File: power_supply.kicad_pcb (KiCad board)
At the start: 2 copper layers, 103.4 x 73 mm, 99 parts, among them J1 USB-IN, J2 USB OUT, Q1 SI4174DY, Q2 SI4463CDY, Q3 SI4463CDY, U1 LM3914, U10 FDC6392S, U11 MCP6041, U2 TPD2E001, U3 MIC2185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

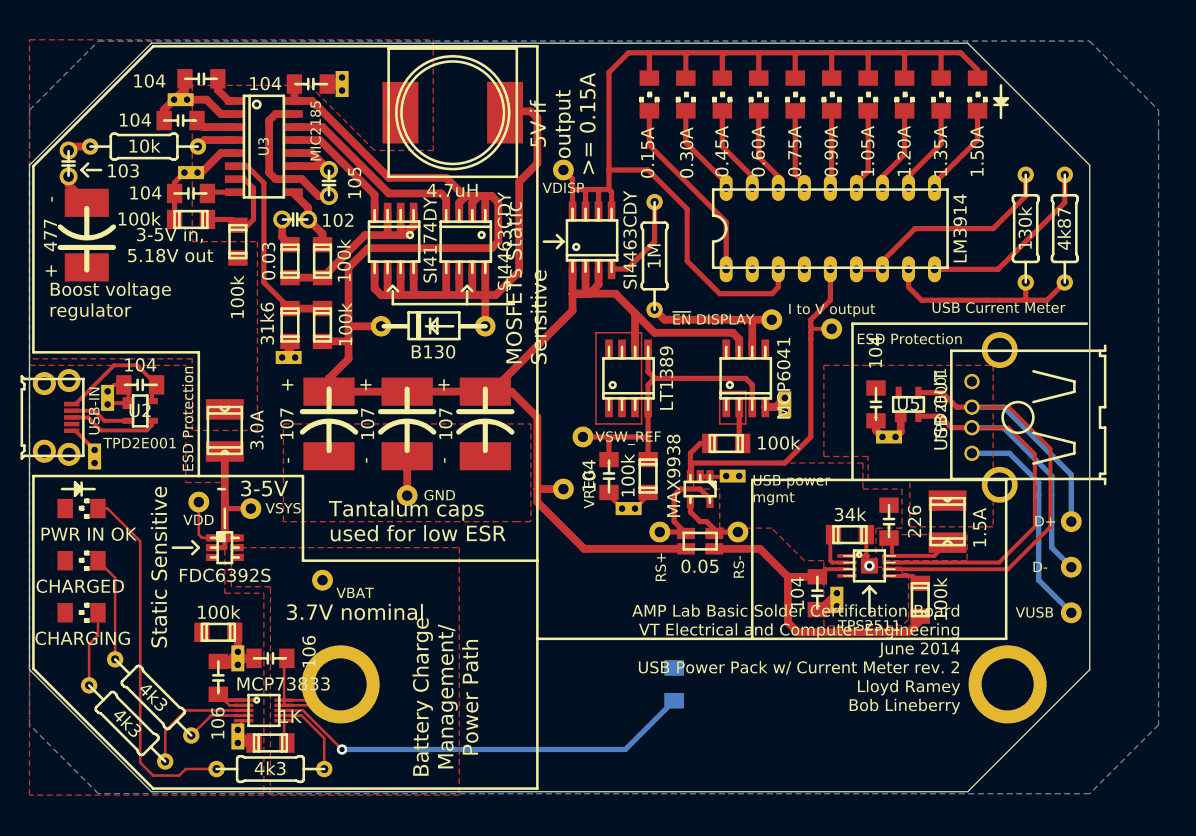
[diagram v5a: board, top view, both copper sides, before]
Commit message: Added test points
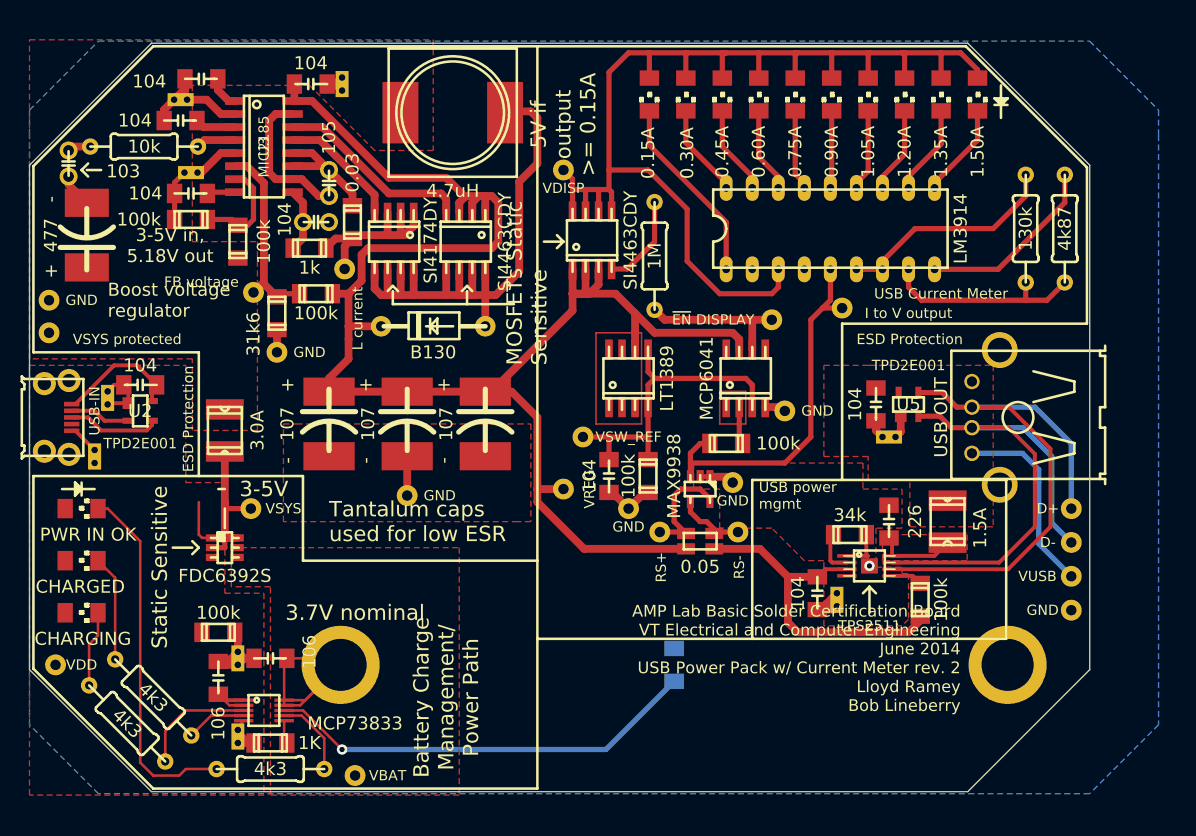
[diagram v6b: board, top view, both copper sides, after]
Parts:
- removed V10, V12, V8, V9: DBL_VIA, DBL_VIA
- added TP15: GND, TP, F.Cu at (154.3, 128.3)
- added TP16: VSYS protected, TP, F.Cu at (154.3, 131.4)
- added TP17: GND, TP, F.Cu at (254.0, 158.5)
- added TP18: GND, TP, F.Cu at (176.5, 133.3)
- added TP19: GND, TP, F.Cu at (210.8, 148.6)
- added TP20: GND, TP, F.Cu at (221.0, 146.1)
- added TP21: GND, TP, F.Cu at (226.1, 139.1)
- added TP22: L current, TP, F.Cu at (183.1, 125.2)
- added TP23: FB voltage, TP, F.Cu at (174.2, 127.5)
- C8: value 102 -> 104
- R9: value 100k -> 1k
- moved TP1 21.1 mm to (154.9, 163.8)
- moved TP6 19.3 mm to (184.2, 174.6)
- moved R10 7.19 mm to (183.9, 120.7)
- moved TP2 3.56 mm to (254.0, 155.2)
- moved R13 3.11 mm to (180.3, 127.6), turned to 0 degrees
- moved TP3 2.41 mm to (254.0, 151.9)
- moved TP8 2.27 mm to (231.6, 129.0)
- moved C8 2.05 mm to (180.3, 120.7), turned to 0 degrees
- moved RT1 1.91 mm to (215.3, 163.8)
- moved U7 1.91 mm to (215.3, 163.8)
- moved R9 1.80 mm to (179.7, 123.2), turned to 180 degrees
- moved R14 1.71 mm to (176.5, 129.5)
- moved TP4 1.27 mm to (254.0, 148.6)
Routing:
- net /VBAT: track 17.2 -> 24.3 mm
- net /VREG: track 195.3 -> 189.9 mm
- net /VUSB_PROTECTED: track 21.7 -> 18.9 mm
- net N-0000064: track 19.9 -> 18.5 mm
- net /D-: track 54.8 -> 53.5 mm
- net N-0000034: track 19.9 -> 18.8 mm
- net N-0000012: track 41.6 -> 42.4 mm
- net /D+: track 56.9 -> 57.4 mm
- net /I_SENSE: track 36.9 -> 36.4 mm
